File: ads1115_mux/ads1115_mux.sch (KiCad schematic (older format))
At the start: 3 parts, among them U4 ADS1115IDGST, U5 CD74HC4067M

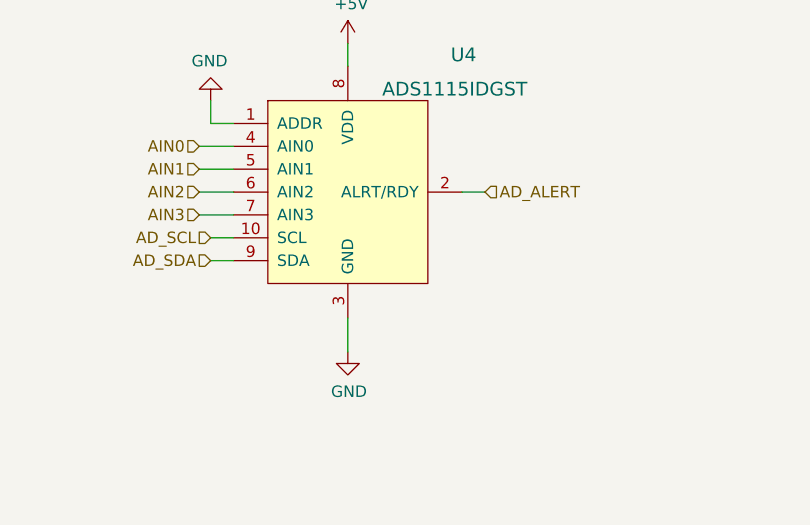
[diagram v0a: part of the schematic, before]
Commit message: Conexão entre os componentes. Correção da lib do buck-boost. Separação do 3v3 da raspberry e do 3v3 do regulador
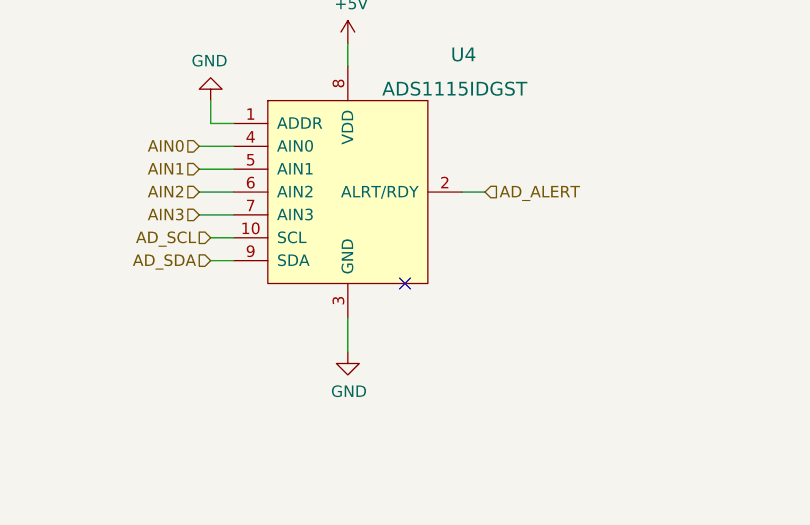
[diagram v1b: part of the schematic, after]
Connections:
- no-connect marks 0 -> 1
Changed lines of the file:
@@
 $EndComp
-Wire Wire Line
-	5200 4200 5200 4350
 Wire Wire Line
 	5200 3000 5200 3100
@@
 	1    0    0    -1
 $EndComp
-Wire Wire Line
-	9600 2850 9600 2950
 Text Notes 650  3600 0    50   ~ 0
 O endereço I2C é selecionado pelo pino ADDR. \nEste pino deve ser conectado ao GND, VSS, SCL ou SDA. \nCada conexão faz com que o CI selecione um endereço.
@@
 $EndComp
 Wire Wire Line
-	8200 4700 8200 4800
-Wire Wire Line
 	7700 4200 7600 4200
 $Comp
@@
 Text HLabel 7700 3100 0    50   Input ~ 0
 AIN0
+Wire Wire Line
+	9600 2850 9600 2950
+NoConn ~ 5450 4050
+Wire Wire Line
+	8200 4700 8200 4800
+Wire Wire Line
+	5200 4200 5200 4350
 $EndSCHEMATC

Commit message: v3
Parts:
- renumbered U4 to U5, U5 to U6
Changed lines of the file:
@@
 $Descr A4 11693 8268
 encoding utf-8
-Sheet 5 7
+Sheet 4 7
 Title ""
 Date "2021-12-26"
@@
 $EndDescr
 $Comp
-L power:GND #PWR0118
+L power:GND #PWR016
 U 1 1 61BD9587
 P 5200 4350
-F 0 "#PWR0118" H 5200 4100 50  0001 C CNN
+F 0 "#PWR016" H 5200 4100 50  0001 C CNN
 F 1 "GND" H 5205 4177 50  0000 C CNN
 F 2 "" H 5200 4350 50  0001 C CNN
@@
 	4700 3350 4600 3350
 $Comp
-L power:GND #PWR0119
+L power:GND #PWR014
 U 1 1 61BDA573
 P 4600 3250
-F 0 "#PWR0119" H 4600 3000 50  0001 C CNN
+F 0 "#PWR014" H 4600 3000 50  0001 C CNN
 F 1 "GND" H 4605 3077 50  0000 C CNN
 F 2 "" H 4600 3250 50  0001 C CNN
@@
 $EndComp
 $Comp
-L power:GND #PWR0120
+L power:GND #PWR021
 U 1 1 61BDC993
 P 9600 2950
-F 0 "#PWR0120" H 9600 2700 50  0001 C CNN
+F 0 "#PWR021" H 9600 2700 50  0001 C CNN
 F 1 "GND" H 9605 2777 50  0000 C CNN
 F 2 "" H 9600 2950 50  0001 C CNN
@@
 	550  4250 550  3200
 $Comp
-L 74xx:CD74HC4067M U5
+L 74xx:CD74HC4067M U6
 U 1 1 61BE2AAD
 P 8200 3600
-F 0 "U5" H 8650 4700 50  0000 C CNN
+F 0 "U6" H 8650 4700 50  0000 C CNN
 F 1 "CD74HC4067M" H 8650 4550 50  0000 C CNN
 F 2 "Package_SO:SOIC-24W_7.5x15.4mm_P1.27mm" H 9100 2600 50  0001 C CIN
@@
 	7700 3800 7600 3800
 $Comp
-L power:GND #PWR0121
+L power:GND #PWR019
 U 1 1 61BE4F67
 P 8200 4800
-F 0 "#PWR0121" H 8200 4550 50  0001 C CNN
+F 0 "#PWR019" H 8200 4550 50  0001 C CNN
 F 1 "GND" H 8205 4627 50  0000 C CNN
 F 2 "" H 8200 4800 50  0001 C CNN
@@
 	7700 4200 7600 4200
 $Comp
-L power:GND #PWR0122
+L power:GND #PWR017
 U 1 1 61BE7A89
 P 7600 4200
-F 0 "#PWR0122" H 7600 3950 50  0001 C CNN
+F 0 "#PWR017" H 7600 3950 50  0001 C CNN
 F 1 "GND" V 7605 4072 50  0000 R CNN
 F 2 "" H 7600 4200 50  0001 C CNN
@@
 AD_SCL
 $Comp
-L power:+5V #PWR0123
+L power:+5V #PWR020
 U 1 1 61DBE0C8
 P 9600 2550
-F 0 "#PWR0123" H 9600 2400 50  0001 C CNN
+F 0 "#PWR020" H 9600 2400 50  0001 C CNN
 F 1 "+5V" H 9615 2723 50  0000 C CNN
 F 2 "" H 9600 2550 50  0001 C CNN
@@
 $EndComp
 $Comp
-L power:+5V #PWR0124
+L power:+5V #PWR018
 U 1 1 61DBF330
 P 8200 2550
-F 0 "#PWR0124" H 8200 2400 50  0001 C CNN
+F 0 "#PWR018" H 8200 2400 50  0001 C CNN
 F 1 "+5V" H 8215 2723 50  0000 C CNN
 F 2 "" H 8200 2550 50  0001 C CNN
@@
 $EndComp
 $Comp
-L power:+5V #PWR0125
+L power:+5V #PWR015
 U 1 1 61DBF85C
 P 5200 3000
-F 0 "#PWR0125" H 5200 2850 50  0001 C CNN
+F 0 "#PWR015" H 5200 2850 50  0001 C CNN
 F 1 "+5V" H 5215 3173 50  0000 C CNN
 F 2 "" H 5200 3000 50  0001 C CNN
@@
 $EndComp
 $Comp
-L dk_Data-Acquisition-Analog-to-Digital-Converters-ADC:ADS1115IDGST U4
+L dk_Data-Acquisition-Analog-to-Digital-Converters-ADC:ADS1115IDGST U5
 U 1 1 61DD285B
 P 5200 3650
-F 0 "U4" H 5650 4250 60  0000 L CNN
+F 0 "U5" H 5650 4250 60  0000 L CNN
 F 1 "ADS1115IDGST" H 5350 4100 60  0000 L CNN
 F 2 "digikey-footprints:MSOP-10_W3mm" H 5400 3850 60  0001 L CNN
